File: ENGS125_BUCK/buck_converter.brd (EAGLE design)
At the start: 75.9 x 62.2 mm, 19 parts, among them M1 IPD220N06L3, M2 IPD220N06L3, U1 LTC6992, U2 LTC4449

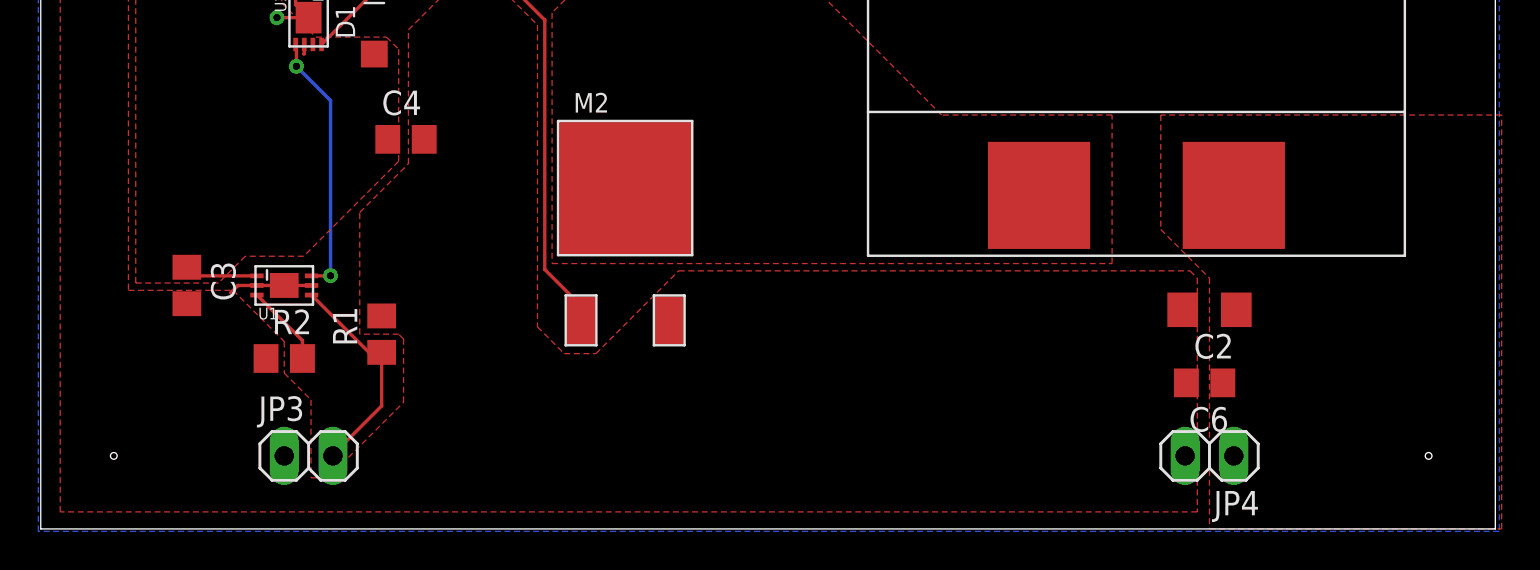
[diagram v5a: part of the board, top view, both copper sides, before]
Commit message: Removed component values from silkscreen
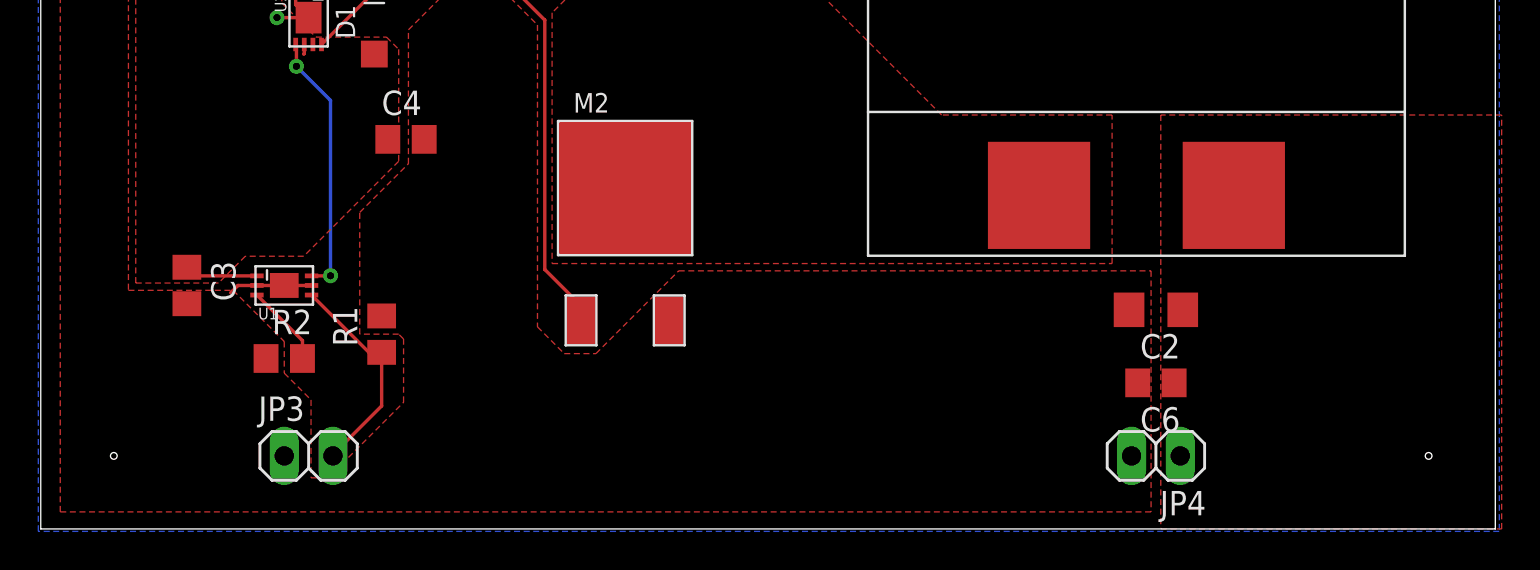
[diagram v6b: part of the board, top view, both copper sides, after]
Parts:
- moved C2 2.79 mm to (58.2, 11.4)
- moved JP4 2.79 mm to (58.2, 3.81)
- moved C6 2.54 mm to (58.2, 7.62)
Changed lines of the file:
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@@
 <element name="C1" library="Engs125_library" package="C0805" value="0.1uF" x="16.51" y="31.75" smashed="yes" rot="R180">
 <attribute name="NAME" x="17.78" y="30.48" size="1.27" layer="25" rot="R180"/>
-<attribute name="VALUE" x="17.78" y="34.29" size="1.27" layer="27" rot="R180"/>
-</element>
-<element name="C2" library="rcl" library_urn="urn:adsk.eagle:library:334" package="C1206" package3d_urn="urn:adsk.eagle:package:23618/2" value="4.7uF" x="60.96" y="11.43" smashed="yes" rot="R180">
-<attribute name="NAME" x="62.23" y="10.16" size="1.27" layer="25" rot="R180"/>
-<attribute name="POPULARITY" value="24" x="26.67" y="43.18" size="1.778" layer="27" rot="R180" display="off"/>
-<attribute name="SPICEPREFIX" value="C" x="26.67" y="43.18" size="1.778" layer="27" rot="R180" display="off"/>
-<attribute name="VALUE" x="62.23" y="13.97" size="1.27" layer="27" rot="R180"/>
+</element>
+<element name="C2" library="rcl" library_urn="urn:adsk.eagle:library:334" package="C1206" package3d_urn="urn:adsk.eagle:package:23618/2" value="4.7uF" x="58.166" y="11.43" smashed="yes" rot="R180">
+<attribute name="NAME" x="59.436" y="10.16" size="1.27" layer="25" rot="R180"/>
+<attribute name="POPULARITY" value="24" x="23.876" y="43.18" size="1.778" layer="27" rot="R180" display="off"/>
+<attribute name="SPICEPREFIX" value="C" x="23.876" y="43.18" size="1.778" layer="27" rot="R180" display="off"/>
 </element>
 <element name="C3" library="Engs125_library" package="C0805" value="1uF" x="7.62" y="12.7" smashed="yes" rot="R270">
 <attribute name="NAME" x="8.89" y="13.97" size="1.27" layer="25" rot="R270"/>
-<attribute name="VALUE" x="5.08" y="13.97" size="1.27" layer="27" rot="R270"/>
 </element>
 <element name="C4" library="Engs125_library" package="C0805" value="1uF" x="19.05" y="20.32" smashed="yes">
 <attribute name="NAME" x="17.78" y="21.59" size="1.27" layer="25"/>
-<attribute name="VALUE" x="17.78" y="17.78" size="1.27" layer="27"/>
 </element>
 <element name="C5" library="rcl" library_urn="urn:adsk.eagle:library:334" package="C1206" package3d_urn="urn:adsk.eagle:package:23618/2" value="4.7uF" x="16.51" y="48.26" smashed="yes" rot="R270">
@@
 <attribute name="POPULARITY" value="24" x="-15.24" y="7.62" size="1.778" layer="27" rot="R270" display="off"/>
 <attribute name="SPICEPREFIX" value="C" x="-15.24" y="7.62" size="1.778" layer="27" rot="R270" display="off"/>
-<attribute name="VALUE" x="13.97" y="49.53" size="1.27" layer="27" rot="R270"/>
-</element>
-<element name="C6" library="Engs125_library" package="C0805" value="1uF" x="60.706" y="7.62" smashed="yes" rot="R180">
-<attribute name="NAME" x="61.976" y="6.35" size="1.27" layer="25" rot="R180"/>
-<attribute name="VALUE" x="61.976" y="10.16" size="1.27" layer="27" rot="R180"/>
+</element>
+<element name="C6" library="Engs125_library" package="C0805" value="1uF" x="58.166" y="7.62" smashed="yes" rot="R180">
+<attribute name="NAME" x="59.436" y="6.35" size="1.27" layer="25" rot="R180"/>
 </element>
 <element name="C7" library="Engs125_library" package="C0805" value="1uF" x="20.32" y="48.26" smashed="yes" rot="R270">
 <attribute name="NAME" x="21.59" y="49.53" size="1.27" layer="25" rot="R270"/>
-<attribute name="VALUE" x="17.78" y="49.53" size="1.27" layer="27" rot="R270"/>
 </element>
 <element name="D1" library="Engs125_library" package="SOD123" value="1N5819" x="17.399" y="26.67" smashed="yes" rot="R90">
 <attribute name="NAME" x="16.399" y="25.57" size="1.016" layer="25" rot="R90"/>
-<attribute name="VALUE" x="19.699" y="25.57" size="1.016" layer="27" rot="R90"/>
 </element>
 <element name="JP1" library="Engs125_library" package="1X02" value="" x="13.97" y="57.15" smashed="yes" rot="R180">
@@
 <attribute name="VALUE" x="11.43" y="0.635" size="1.27" layer="27"/>
 </element>
-<element name="JP4" library="Engs125_library" package="1X02" value="" x="60.96" y="3.81" smashed="yes" rot="R180">
-<attribute name="NAME" x="63.5762" y="1.9812" size="1.27" layer="25" ratio="10" rot="R180"/>
-<attribute name="VALUE" x="63.5" y="6.985" size="1.27" layer="27" rot="R180"/>
+<element name="JP4" library="Engs125_library" package="1X02" value="" x="58.166" y="3.81" smashed="yes" rot="R180">
+<attribute name="NAME" x="60.7822" y="1.9812" size="1.27" layer="25" ratio="10" rot="R180"/>
+<attribute name="VALUE" x="60.706" y="6.985" size="1.27" layer="27" rot="R180"/>
 </element>
 <element name="L1" library="Engs125_library" package="SER2900" value="4.7uH" x="57.15" y="31.75" smashed="yes">
 <attribute name="NAME" x="53.34" y="27.94" size="1.27" layer="25"/>
-<attribute name="VALUE" x="53.34" y="33.02" size="1.27" layer="27"/>
 </element>
 <element name="M1" library="Engs125_library" package="DPAK" value="IPD220N06L3" x="30.48" y="38.1" smashed="yes">
 <attribute name="NAME" x="27.78" y="42.04" size="1.016" layer="25"/>
-<attribute name="VALUE" x="35.4" y="35.99" size="1.016" layer="27" rot="R90"/>
 </element>
 <element name="M2" library="Engs125_library" package="DPAK" value="IPD220N06L3" x="30.48" y="17.78" smashed="yes">
 <attribute name="NAME" x="27.78" y="21.72" size="1.016" layer="25"/>
-<attribute name="VALUE" x="35.4" y="15.67" size="1.016" layer="27" rot="R90"/>
 </element>
 <element name="R1" library="Engs125_library" package="R0805" value="1kΩ" x="17.78" y="10.16" smashed="yes" rot="R90">
 <attribute name="NAME" x="16.51" y="9.525" size="1.27" layer="25" rot="R90"/>
-<attribute name="VALUE" x="20.32" y="9.525" size="1.27" layer="27" rot="R90"/>
 </element>
 <element name="R2" library="Engs125_library" package="R0805" value="100kΩ" x="12.7" y="8.89" smashed="yes">
 <attribute name="NAME" x="12.065" y="10.16" size="1.27" layer="25"/>
-<attribute name="VALUE" x="12.065" y="6.35" size="1.27" layer="27"/>
 </element>
 <element name="U1" library="Engs125_library" package="LTC6992" value="LTC6992" x="12.7" y="12.7" smashed="yes" rot="R270">
 <attribute name="NAME" x="11.34" y="10.93" size="0.6096" layer="25"/>
-<attribute name="VALUE" x="11.34" y="13.9" size="0.6096" layer="27"/>
 </element>
 <element name="U2" library="Engs125_library" package="DCB8" value="LTC4449" x="13.97" y="26.67" smashed="yes" rot="R180">
@@
 <via x="12.319" y="26.67" extent="1-16" drill="0.381"/>
 <polygon width="0.1778" layer="1" isolate="0.00030625" thermals="no">
-<vertex x="60.325" y="13.081"/>
-<vertex x="60.325" y="0.889"/>
+<vertex x="57.912" y="13.462"/>
+<vertex x="57.912" y="0.889"/>
 <vertex x="1.016" y="0.889"/>
 <vertex x="1.016" y="61.087"/>
@@
 <vertex x="28.956" y="9.144"/>
 <vertex x="33.274" y="13.462"/>
-<vertex x="59.944" y="13.462"/>
 </polygon>
 <wire x1="11.275" y1="12.7" x2="10.287" y2="12.7" width="0.1778" layer="1"/>
@@
 <polygon width="0.1524" layer="1" isolate="0.00030625" thermals="no">
 <vertex x="58.42" y="21.59"/>
-<vertex x="58.42" y="15.621"/>
-<vertex x="60.96" y="13.081"/>
-<vertex x="60.96" y="0"/>
+<vertex x="58.42" y="0"/>
 <vertex x="76.2" y="0"/>
 <vertex x="76.2" y="21.59"/>

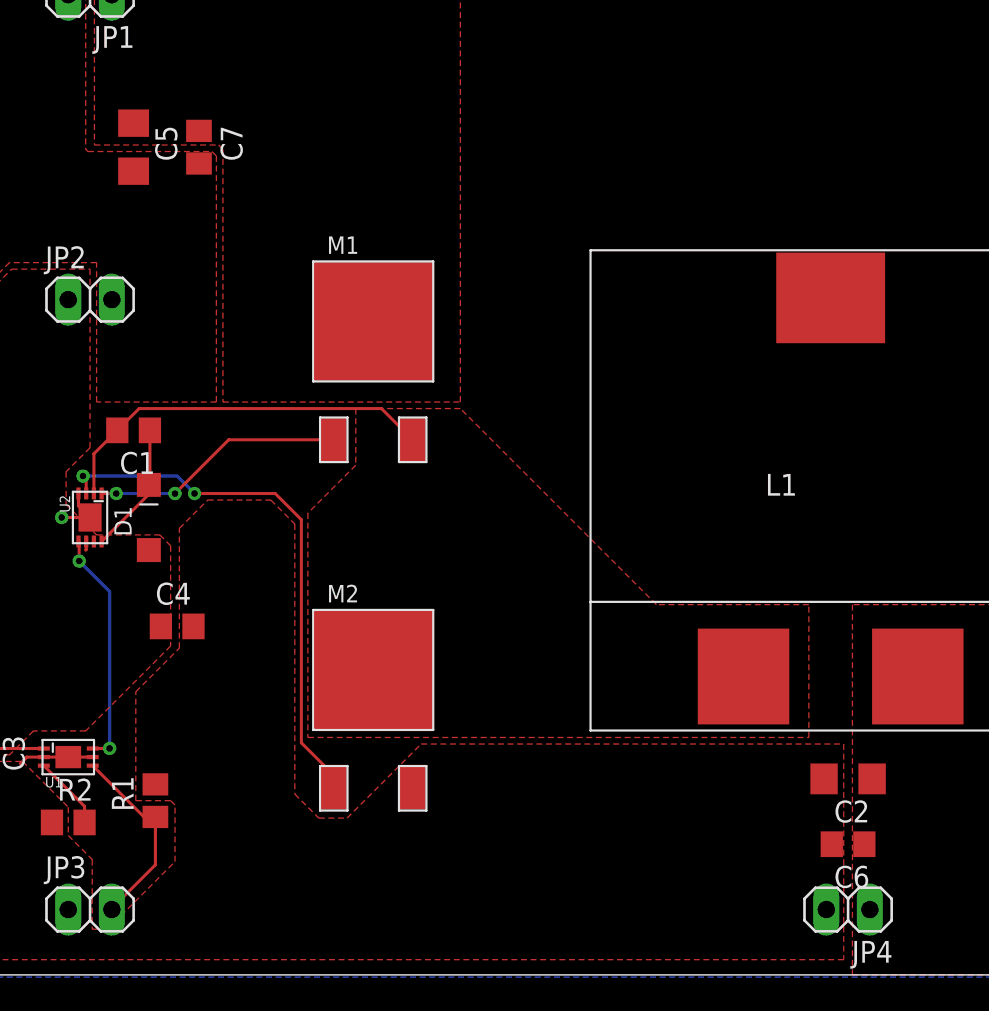
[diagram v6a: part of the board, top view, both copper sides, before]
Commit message: Added grounding vias
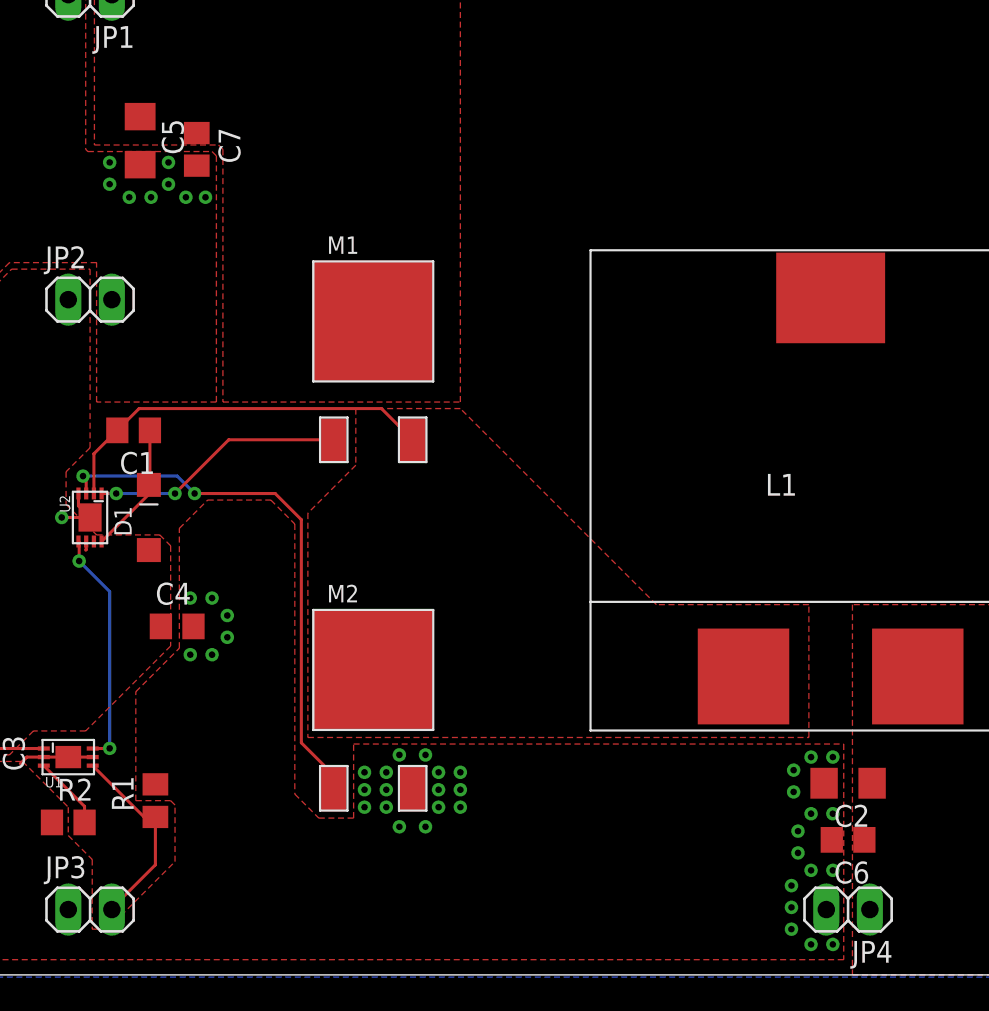
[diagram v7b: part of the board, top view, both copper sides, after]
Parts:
- moved C5 0.54 mm to (16.9, 48.6)
- moved C2 0.25 mm to (58.2, 11.2)
- moved C6 0.25 mm to (58.2, 7.87)
- moved C7 0.18 mm to (20.2, 48.1)
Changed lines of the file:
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@@
 <attribute name="NAME" x="17.78" y="30.48" size="1.27" layer="25" rot="R180"/>
 </element>
-<element name="C2" library="rcl" library_urn="urn:adsk.eagle:library:334" package="C1206" package3d_urn="urn:adsk.eagle:package:23618/2" value="4.7uF" x="58.166" y="11.43" smashed="yes" rot="R180">
-<attribute name="NAME" x="59.436" y="10.16" size="1.27" layer="25" rot="R180"/>
-<attribute name="POPULARITY" value="24" x="23.876" y="43.18" size="1.778" layer="27" rot="R180" display="off"/>
-<attribute name="SPICEPREFIX" value="C" x="23.876" y="43.18" size="1.778" layer="27" rot="R180" display="off"/>
+<element name="C2" library="rcl" library_urn="urn:adsk.eagle:library:334" package="C1206" package3d_urn="urn:adsk.eagle:package:23618/2" value="4.7uF" x="58.166" y="11.176" smashed="yes" rot="R180">
+<attribute name="NAME" x="59.436" y="9.906" size="1.27" layer="25" rot="R180"/>
+<attribute name="POPULARITY" value="24" x="23.876" y="42.926" size="1.778" layer="27" rot="R180" display="off"/>
+<attribute name="SPICEPREFIX" value="C" x="23.876" y="42.926" size="1.778" layer="27" rot="R180" display="off"/>
 </element>
 <element name="C3" library="Engs125_library" package="C0805" value="1uF" x="7.62" y="12.7" smashed="yes" rot="R270">
@@
 <attribute name="NAME" x="17.78" y="21.59" size="1.27" layer="25"/>
 </element>
-<element name="C5" library="rcl" library_urn="urn:adsk.eagle:library:334" package="C1206" package3d_urn="urn:adsk.eagle:package:23618/2" value="4.7uF" x="16.51" y="48.26" smashed="yes" rot="R270">
-<attribute name="NAME" x="17.78" y="49.53" size="1.27" layer="25" rot="R270"/>
-<attribute name="POPULARITY" value="24" x="-15.24" y="7.62" size="1.778" layer="27" rot="R270" display="off"/>
-<attribute name="SPICEPREFIX" value="C" x="-15.24" y="7.62" size="1.778" layer="27" rot="R270" display="off"/>
-</element>
-<element name="C6" library="Engs125_library" package="C0805" value="1uF" x="58.166" y="7.62" smashed="yes" rot="R180">
-<attribute name="NAME" x="59.436" y="6.35" size="1.27" layer="25" rot="R180"/>
-</element>
-<element name="C7" library="Engs125_library" package="C0805" value="1uF" x="20.32" y="48.26" smashed="yes" rot="R270">
-<attribute name="NAME" x="21.59" y="49.53" size="1.27" layer="25" rot="R270"/>
+<element name="C5" library="rcl" library_urn="urn:adsk.eagle:library:334" package="C1206" package3d_urn="urn:adsk.eagle:package:23618/2" value="4.7uF" x="16.891" y="48.641" smashed="yes" rot="R270">
+<attribute name="NAME" x="18.161" y="49.911" size="1.27" layer="25" rot="R270"/>
+<attribute name="POPULARITY" value="24" x="-14.859" y="8.001" size="1.778" layer="27" rot="R270" display="off"/>
+<attribute name="SPICEPREFIX" value="C" x="-14.859" y="8.001" size="1.778" layer="27" rot="R270" display="off"/>
+</element>
+<element name="C6" library="Engs125_library" package="C0805" value="1uF" x="58.166" y="7.874" smashed="yes" rot="R180">
+<attribute name="NAME" x="59.436" y="6.604" size="1.27" layer="25" rot="R180"/>
+</element>
+<element name="C7" library="Engs125_library" package="C0805" value="1uF" x="20.193" y="48.133" smashed="yes" rot="R270">
+<attribute name="NAME" x="21.463" y="49.403" size="1.27" layer="25" rot="R270"/>
 </element>
 <element name="D1" library="Engs125_library" package="SOD123" value="1N5819" x="17.399" y="26.67" smashed="yes" rot="R90">
@@
 <vertex x="25.908" y="10.541"/>
 <vertex x="27.305" y="9.144"/>
-<vertex x="28.956" y="9.144"/>
-<vertex x="33.274" y="13.462"/>
+<vertex x="29.337" y="9.144"/>
+<vertex x="29.337" y="13.462"/>
 </polygon>
 <wire x1="11.275" y1="12.7" x2="10.287" y2="12.7" width="0.1778" layer="1"/>
@@
 <wire x1="14.648" y1="28.067" x2="14.645" y2="28.07" width="0.1778" layer="1"/>
 </signal>
+<signal name="N$3">
+<via x="29.972" y="11.811" extent="1-16" drill="0.381"/>
+</signal>
+<signal name="N$4">
+<via x="31.242" y="11.811" extent="1-16" drill="0.381"/>
+</signal>
+<signal name="N$5">
+<via x="29.972" y="10.795" extent="1-16" drill="0.381"/>
+</signal>
+<signal name="N$6">
+<via x="31.242" y="10.795" extent="1-16" drill="0.381"/>
+</signal>
+<signal name="N$7">
+<via x="29.972" y="9.779" extent="1-16" drill="0.381"/>
+</signal>
+<signal name="N$8">
+<via x="31.242" y="9.779" extent="1-16" drill="0.381"/>
+</signal>
+<signal name="N$9">
+<via x="34.29" y="11.811" extent="1-16" drill="0.381"/>
+</signal>
+<signal name="N$10">
+<via x="35.56" y="11.811" extent="1-16" drill="0.381"/>
+</signal>
+<signal name="N$11">
+<via x="34.29" y="10.795" extent="1-16" drill="0.381"/>
+</signal>
+<signal name="N$12">
+<via x="35.56" y="10.795" extent="1-16" drill="0.381"/>
+</signal>
+<signal name="N$13">
+<via x="34.29" y="9.779" extent="1-16" drill="0.381"/>
+</signal>
+<signal name="N$14">
+<via x="35.56" y="9.779" extent="1-16" drill="0.381"/>
+</signal>
+<signal name="N$17">
+<via x="32.004" y="12.827" extent="1-16" drill="0.381"/>
+</signal>
+<signal name="N$18">
+<via x="33.528" y="12.827" extent="1-16" drill="0.381"/>
+</signal>
+<signal name="N$20">
+<via x="32.004" y="8.636" extent="1-16" drill="0.381"/>
+</signal>
+<signal name="N$21">
+<via x="33.528" y="8.636" extent="1-16" drill="0.381"/>
+</signal>
+<signal name="N$15">
+<via x="57.277" y="9.398" extent="1-16" drill="0.381"/>
+</signal>
+<signal name="N$16">
+<via x="56.007" y="9.398" extent="1-16" drill="0.381"/>
+</signal>
+<signal name="N$19">
+<via x="55.245" y="8.382" extent="1-16" drill="0.381"/>
+</signal>
+<signal name="N$22">
+<via x="55.245" y="7.112" extent="1-16" drill="0.381"/>
+</signal>
+<signal name="N$23">
+<via x="56.007" y="6.096" extent="1-16" drill="0.381"/>
+</signal>
+<signal name="N$24">
+<via x="57.277" y="6.096" extent="1-16" drill="0.381"/>
+</signal>
+<signal name="N$25">
+<via x="57.277" y="12.7" extent="1-16" drill="0.381"/>
+</signal>
+<signal name="N$26">
+<via x="56.007" y="12.7" extent="1-16" drill="0.381"/>
+</signal>
+<signal name="N$27">
+<via x="54.991" y="11.938" extent="1-16" drill="0.381"/>
+</signal>
+<signal name="N$28">
+<via x="54.991" y="10.668" extent="1-16" drill="0.381"/>
+</signal>
+<signal name="N$29">
+<via x="54.864" y="5.207" extent="1-16" drill="0.381"/>
+</signal>
+<signal name="N$30">
+<via x="54.864" y="3.937" extent="1-16" drill="0.381"/>
+</signal>
+<signal name="N$31">
+<via x="54.864" y="2.667" extent="1-16" drill="0.381"/>
+</signal>
+<signal name="N$32">
+<via x="57.277" y="1.778" extent="1-16" drill="0.381"/>
+</signal>
+<signal name="N$33">
+<via x="56.007" y="1.778" extent="1-16" drill="0.381"/>
+</signal>
+<signal name="N$34">
+<via x="19.812" y="21.971" extent="1-16" drill="0.381"/>
+</signal>
+<signal name="N$35">
+<via x="19.812" y="18.669" extent="1-16" drill="0.381"/>
+</signal>
+<signal name="N$36">
+<via x="21.082" y="18.669" extent="1-16" drill="0.381"/>
+</signal>
+<signal name="N$37">
+<via x="21.971" y="19.685" extent="1-16" drill="0.381"/>
+</signal>
+<signal name="N$38">
+<via x="21.971" y="20.955" extent="1-16" drill="0.381"/>
+</signal>
+<signal name="N$39">
+<via x="21.082" y="21.971" extent="1-16" drill="0.381"/>
+</signal>
+<signal name="N$40">
+<via x="18.542" y="47.371" extent="1-16" drill="0.381"/>
+</signal>
+<signal name="N$42">
+<via x="20.701" y="45.339" extent="1-16" drill="0.381"/>
+</signal>
+<signal name="N$43">
+<via x="19.558" y="45.339" extent="1-16" drill="0.381"/>
+</signal>
+<signal name="N$41">
+<via x="15.113" y="47.371" extent="1-16" drill="0.381"/>
+</signal>
+<signal name="N$45">
+<via x="15.113" y="46.101" extent="1-16" drill="0.381"/>
+</signal>
+<signal name="N$46">
+<via x="16.256" y="45.339" extent="1-16" drill="0.381"/>
+</signal>
+<signal name="N$47">
+<via x="17.526" y="45.339" extent="1-16" drill="0.381"/>
+</signal>
+<signal name="N$44">
+<via x="18.542" y="46.101" extent="1-16" drill="0.381"/>
+</signal>
 </signals>
